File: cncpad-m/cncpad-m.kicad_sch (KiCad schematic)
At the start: 27 parts, among them J1 Conn_01x04_Male - Encoder, SW1 SW_PUSH, SW2 SW_PUSH, SW3 SW_PUSH, SW4 SW_PUSH, SW5 SW_PUSH, SW6 SW_PUSH, SW7 SW_PUSH, SW8 SW_PUSH, SW9 SW_PUSH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

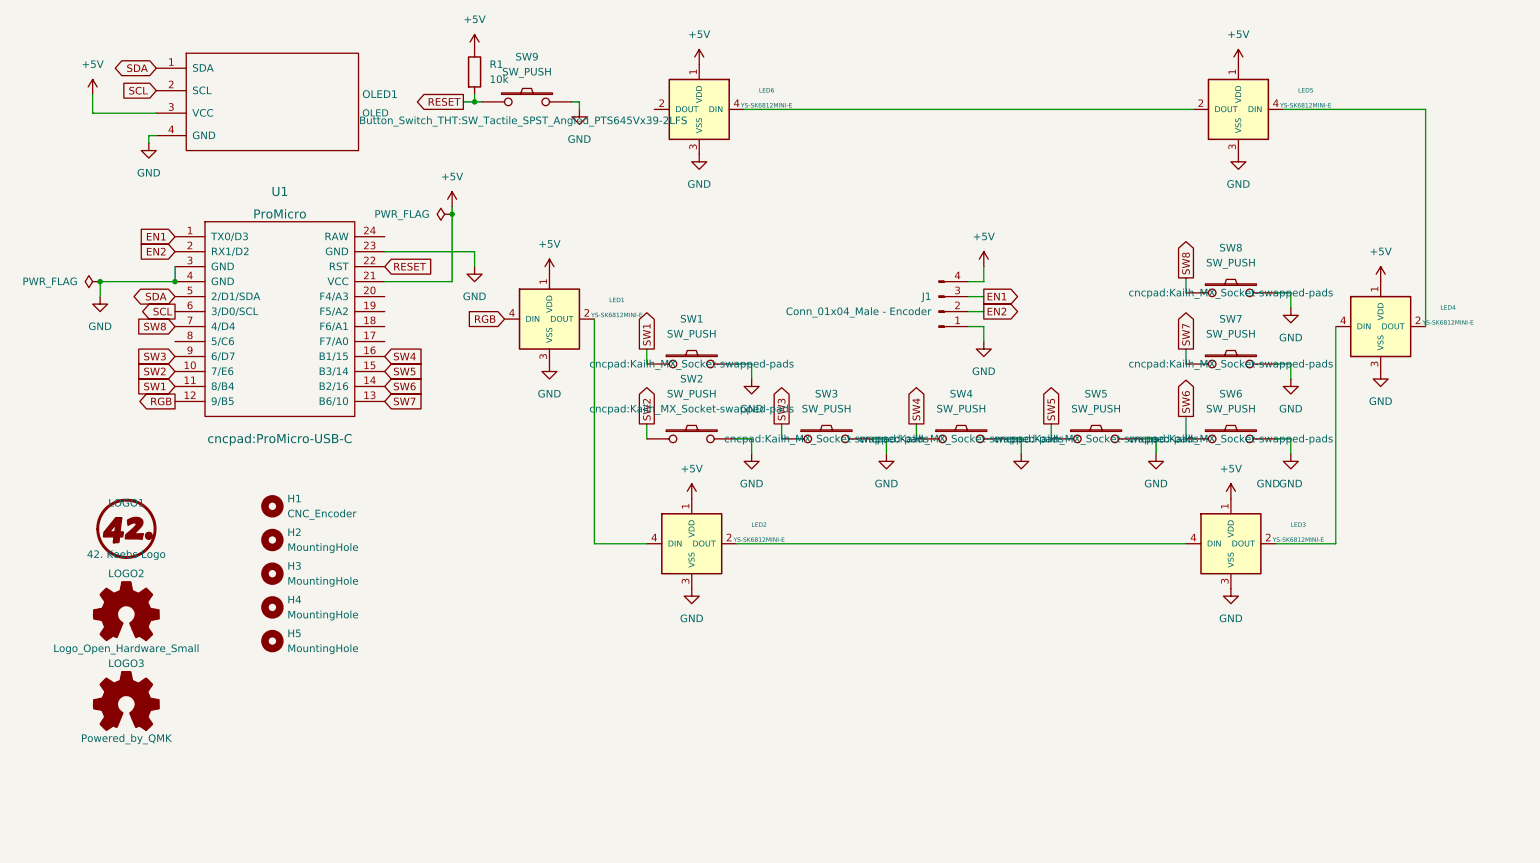
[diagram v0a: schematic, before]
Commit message: Add missing I2C pullups; change encoder header
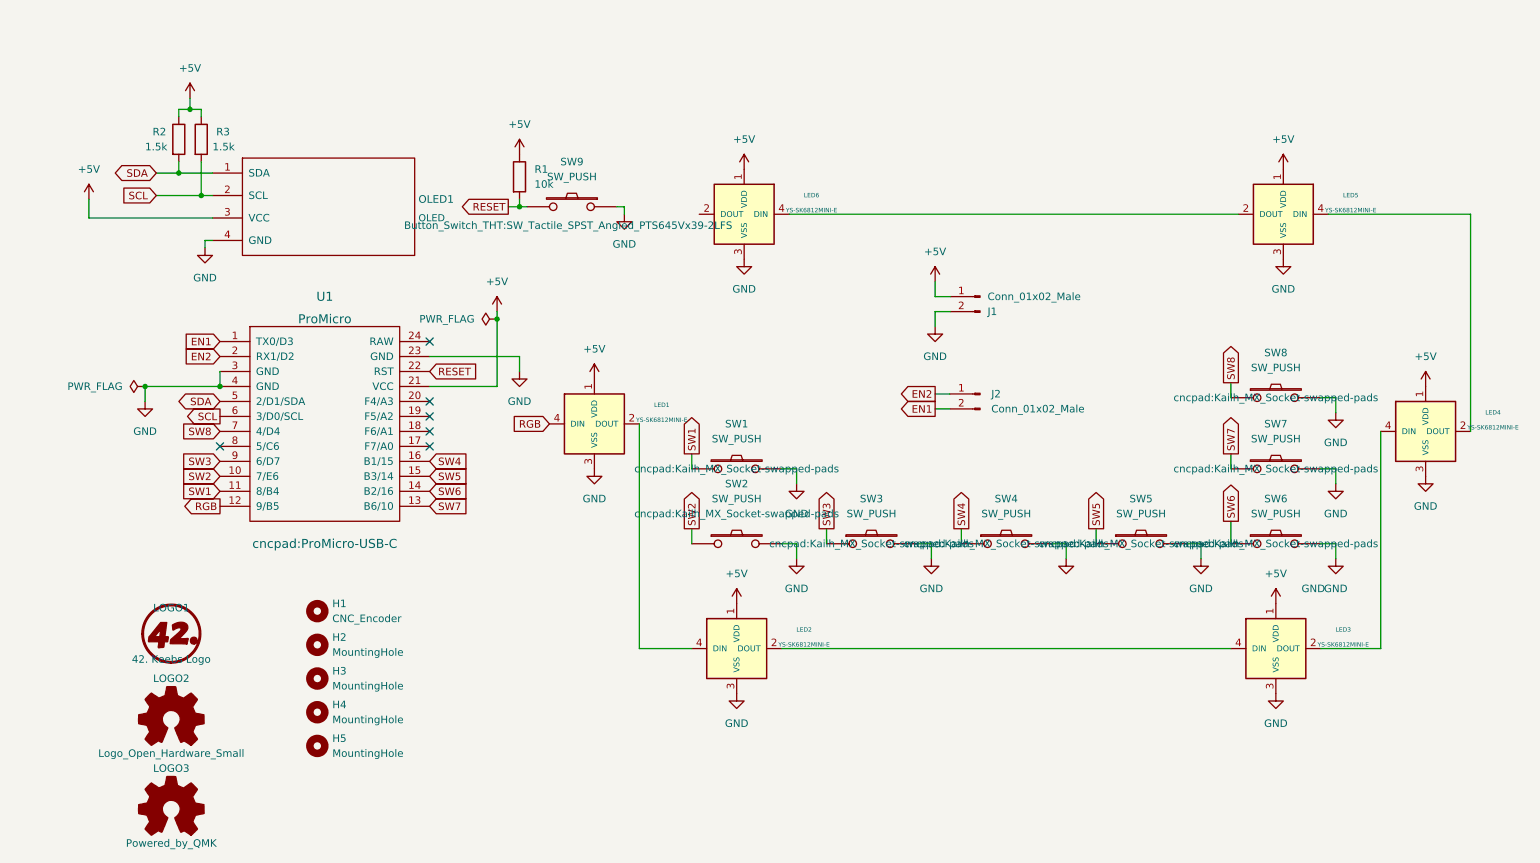
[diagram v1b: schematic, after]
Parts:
- removed J1: Conn_01x04_Male - Encoder, Connector_PinHeader_2.54mm:PinHeader_1x04_P2.54mm_Horizontal, symbol Connector:Conn_01x04_Male
- added J1, J2: Conn_01x02_Male, Connector_PinHeader_2.54mm:PinHeader_1x02_P2.54mm_Horizontal, symbol Connector:Conn_01x02_Male
- added R2, R3: 1.5k, Resistor_THT:R_Axial_DIN0204_L3.6mm_D1.6mm_P5.08mm_Horizontal, symbol Device:R
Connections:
- net +5V: now also J1.1 (Pin_1), R2.1, R3.1
- net EN1: now also J2.2 (Pin_2)
- net EN2: now also J2.1 (Pin_1)
- net GND: now also J1.2 (Pin_2)
- net SCL: now also R3.2
- net SDA: now also R2.2
- no-connect marks 0 -> 6
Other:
- moved on the sheet: H1, H2, H3, H4, H5, LED1, LED2, LED3, LED4, LED5, LED6, LOGO1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
